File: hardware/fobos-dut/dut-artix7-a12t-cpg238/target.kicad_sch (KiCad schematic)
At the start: 39 parts, among them J1 Target, J2 Pmod 2x6, U1 TS3A5018DBQR, U2 SP3003-04ATG, U3 SP3003-04ATG, U4 SP3003-04ATG, U5 SP3003-04ATG, U6 SP3003-04ATG

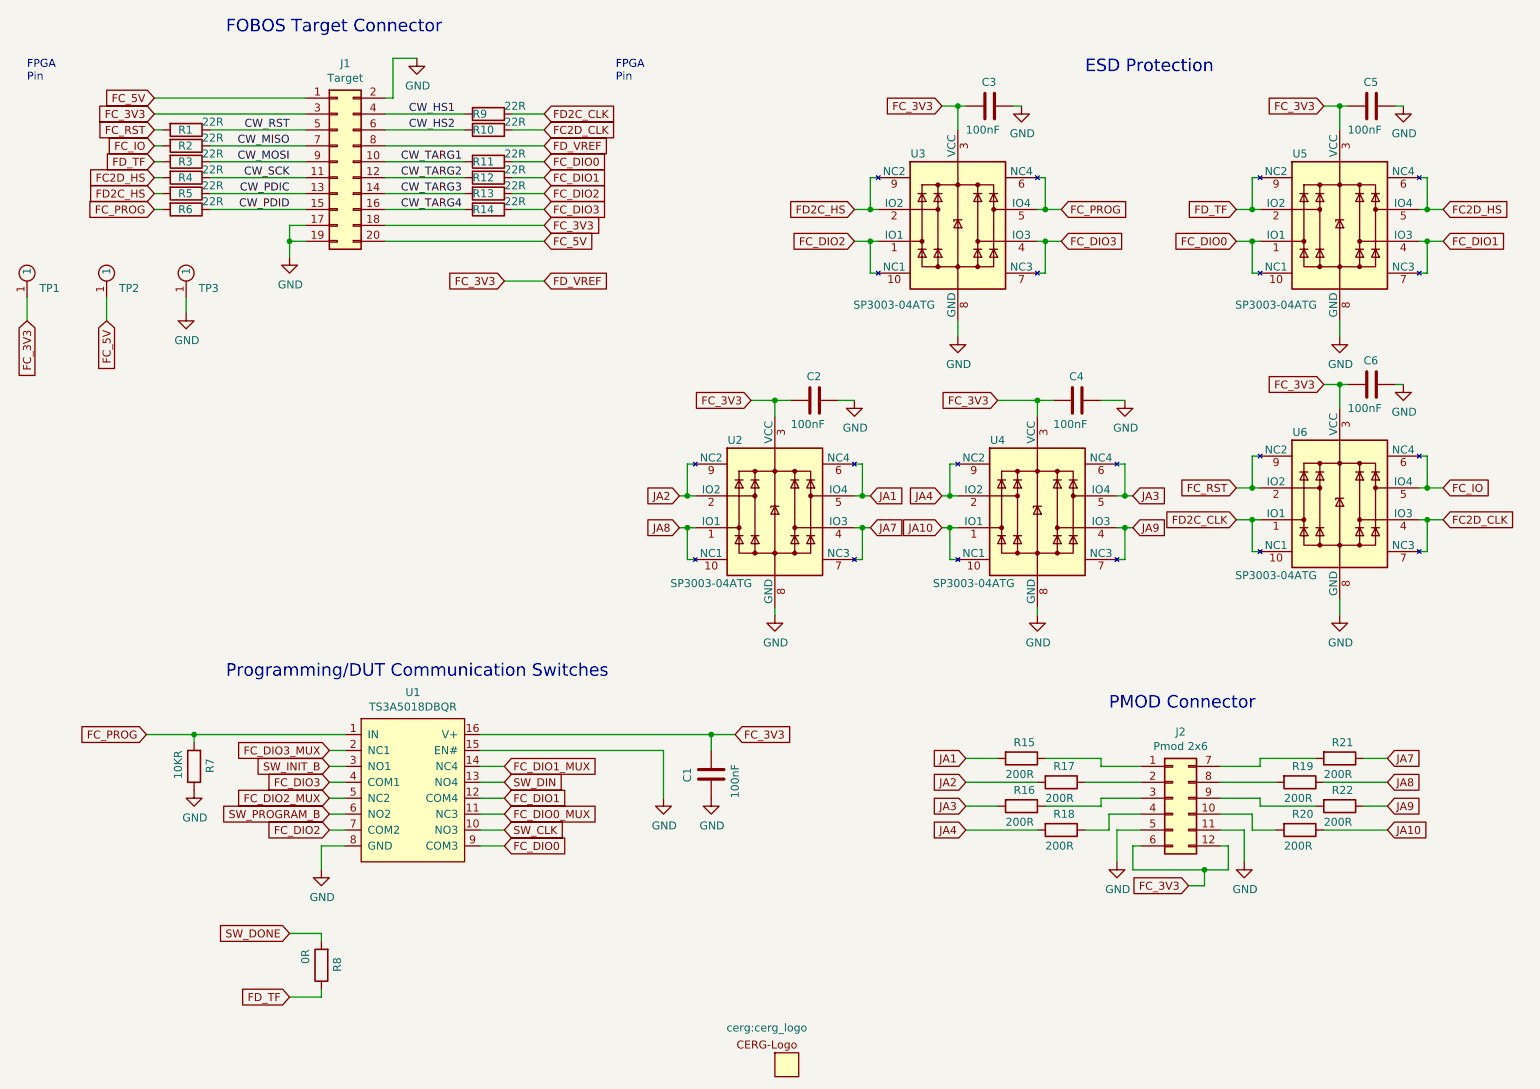
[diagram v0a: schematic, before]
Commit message: cleaned up FBDA7 rev1 added BOM, fixed bugs in schematic
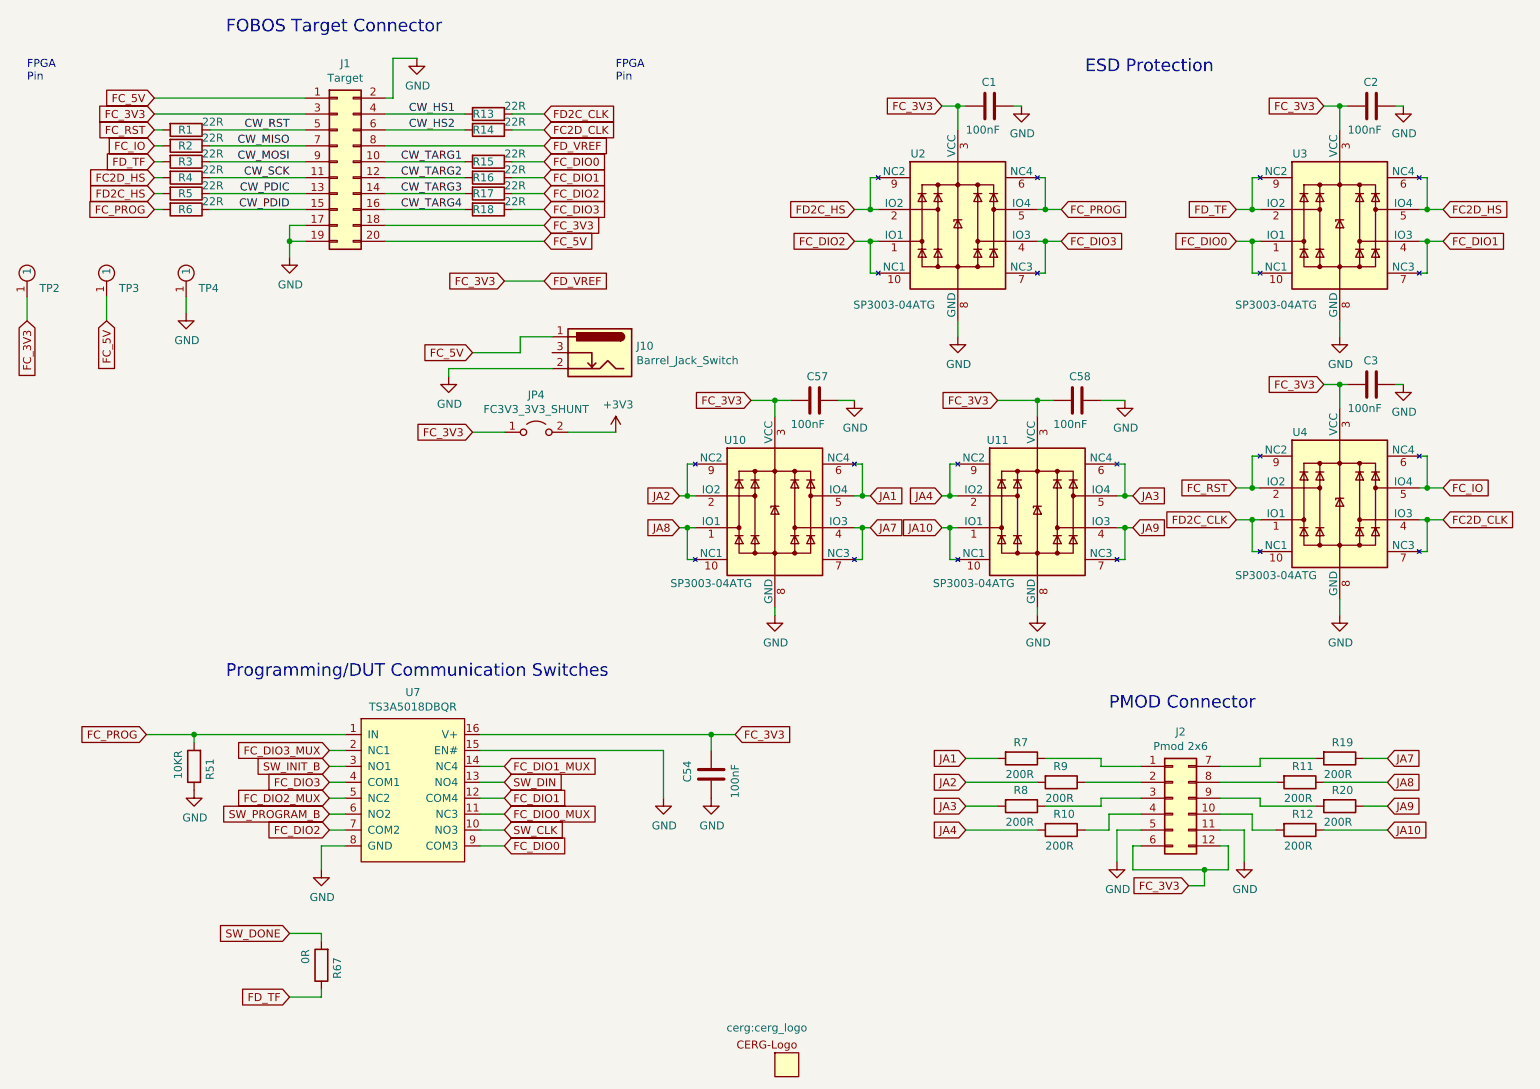
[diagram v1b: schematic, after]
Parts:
- added J10: Barrel_Jack_Switch, cerg:BarrelJack_CUI_PJ-102AH_Horizontal, symbol Connector:Barrel_Jack_Switch
- added JP4: FC3V3_3V3_SHUNT, Connector_PinHeader_2.54mm:PinHeader_1x02_P2.54mm_Vertical, symbol Jumper:Jumper_2_Open
- renumbered C3 to C1, C5 to C2, C6 to C3, C1 to C54, C2 to C57, C4 to C58, R18 to R10, R19 to R11, R20 to R12, R9 to R13, R10 to R14, R11 to R15, R12 to R16, R13 to R17, R14 to R18, R21 to R19, R22 to R20, R7 to R51, R8 to R67, R15 to R7, R16 to R8, R17 to R9, TP1 to TP2, TP2 to TP3, TP3 to TP4, U2 to U10, U4 to U11, U3 to U2, U5 to U3, U6 to U4, U1 to U7
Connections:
- net FC_3V3: now also JP4.1 (A)
- net FC_5V: now also J10.1
- net GND: now also J10.2
- new net +3V3: JP4.2 (B)
